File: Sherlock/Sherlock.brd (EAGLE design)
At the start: 91.1 x 58.4 mm, 25 parts, among them U3 XBEE-1B2, X1 2540-

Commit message: Added resistor values for R1-R4 for Sherlock
Change-Id: Ic35e8ce0279ecb8ac04751f8d59191d34fd62b27
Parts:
- R1, R2, R3, R4: value (none) -> 330
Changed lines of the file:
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@@
 <?xml version="1.0" encoding="utf-8"?>
 <!DOCTYPE eagle SYSTEM "eagle.dtd">
-<eagle version="6.2">
+<eagle version="6.3">
 <drawing>
 <settings>
@@
 </class>
 </classes>
-<designrules>
+<designrules name="advancedcircuits-33each-pie">
 <description language="de">&lt;b&gt;EAGLE Design Rules&lt;/b&gt;
 &lt;p&gt;
@@
 <attribute name="VALUE" x="70.485" y="52.07" size="1.27" layer="27" rot="R270"/>
 </element>
-<element name="R1" library="rcl" package="R0603" value="" x="29.21" y="2.54" smashed="yes" rot="MR90">
+<element name="R1" library="rcl" package="R0603" value="330" x="29.21" y="2.54" smashed="yes" rot="MR90">
 <attribute name="NAME" x="30.099" y="7.493" size="1.4224" layer="26" font="vector" ratio="15" rot="MR0"/>
-<attribute name="VALUE" x="27.305" y="1.905" size="1.27" layer="28" rot="MR90"/>
-</element>
-<element name="R2" library="rcl" package="R0603" value="" x="17.78" y="2.54" smashed="yes" rot="MR90">
+<attribute name="VALUE" x="29.845" y="-1.016" size="1.4224" layer="28" rot="MR0"/>
+</element>
+<element name="R2" library="rcl" package="R0603" value="330" x="17.78" y="2.54" smashed="yes" rot="MR90">
 <attribute name="NAME" x="18.669" y="7.62" size="1.4224" layer="26" font="vector" ratio="15" rot="MR0"/>
-<attribute name="VALUE" x="15.875" y="1.905" size="1.27" layer="28" rot="MR90"/>
-</element>
-<element name="R3" library="rcl" package="R0603" value="" x="21.59" y="2.54" smashed="yes" rot="MR90">
+<attribute name="VALUE" x="18.415" y="-1.016" size="1.4224" layer="28" rot="MR0"/>
+</element>
+<element name="R3" library="rcl" package="R0603" value="330" x="21.59" y="2.54" smashed="yes" rot="MR90">
 <attribute name="NAME" x="22.606" y="7.493" size="1.4224" layer="26" font="vector" ratio="15" rot="MR0"/>
-<attribute name="VALUE" x="19.685" y="1.905" size="1.27" layer="28" rot="MR90"/>
-</element>
-<element name="R4" library="rcl" package="R0603" value="" x="25.4" y="2.54" smashed="yes" rot="MR90">
+<attribute name="VALUE" x="22.225" y="-1.016" size="1.4224" layer="28" rot="MR0"/>
+</element>
+<element name="R4" library="rcl" package="R0603" value="330" x="25.4" y="2.54" smashed="yes" rot="MR90">
 <attribute name="NAME" x="26.162" y="7.493" size="1.4224" layer="26" font="vector" ratio="15" rot="MR0"/>
-<attribute name="VALUE" x="23.495" y="1.905" size="1.27" layer="28" rot="MR90"/>
+<attribute name="VALUE" x="26.035" y="-1.016" size="1.4224" layer="28" rot="MR0"/>
 </element>
 <element name="C3" library="rcl" package="C0603K" value=".1uF" x="41.91" y="19.05" smashed="yes" rot="MR0">

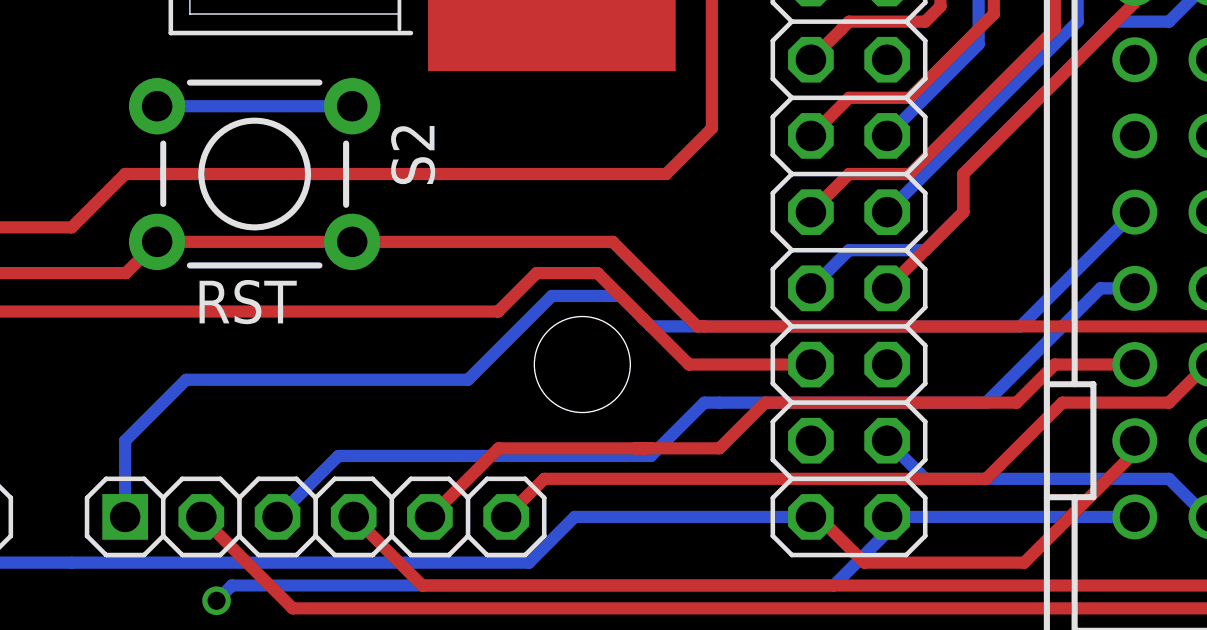
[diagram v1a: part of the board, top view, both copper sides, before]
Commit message: Moved traces away from hole on Sherlock
Change-Id: Icbd6ea3e393f3e41c299999c4f7f65ddeaf7ec65
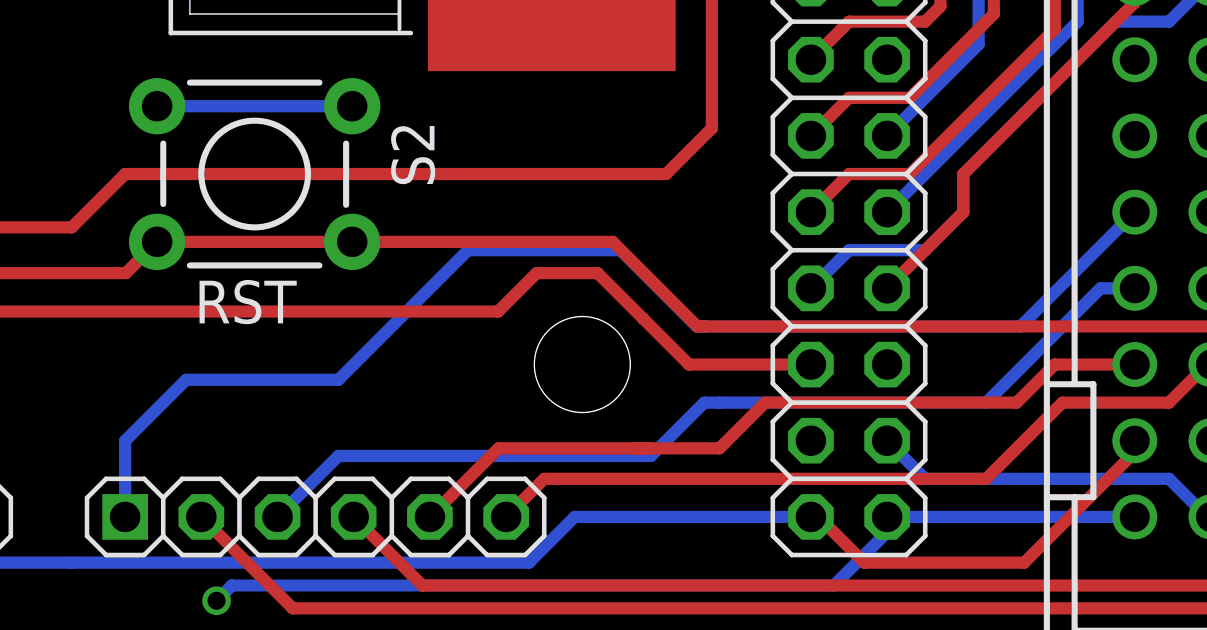
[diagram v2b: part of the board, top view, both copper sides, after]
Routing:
- net ADC0/IO28*: track 40.2 -> 41.5 mm
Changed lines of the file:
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@@
 <grid distance="0.05" unitdist="inch" unit="inch" style="lines" multiple="1" display="yes" altdistance="0.025" altunitdist="inch" altunit="inch"/>
 <layers>
-<layer number="1" name="Top" color="4" fill="1" visible="no" active="yes"/>
+<layer number="1" name="Top" color="4" fill="1" visible="yes" active="yes"/>
 <layer number="16" name="Bottom" color="1" fill="1" visible="yes" active="yes"/>
 <layer number="17" name="Pads" color="2" fill="1" visible="yes" active="yes"/>
@@
 <layer number="19" name="Unrouted" color="6" fill="1" visible="yes" active="yes"/>
 <layer number="20" name="Dimension" color="15" fill="1" visible="yes" active="yes"/>
-<layer number="21" name="tPlace" color="7" fill="1" visible="no" active="yes"/>
+<layer number="21" name="tPlace" color="7" fill="1" visible="yes" active="yes"/>
 <layer number="22" name="bPlace" color="7" fill="1" visible="yes" active="yes"/>
-<layer number="23" name="tOrigins" color="15" fill="1" visible="no" active="yes"/>
+<layer number="23" name="tOrigins" color="15" fill="1" visible="yes" active="yes"/>
 <layer number="24" name="bOrigins" color="15" fill="1" visible="yes" active="yes"/>
-<layer number="25" name="tNames" color="7" fill="1" visible="no" active="yes"/>
+<layer number="25" name="tNames" color="7" fill="1" visible="yes" active="yes"/>
 <layer number="26" name="bNames" color="7" fill="1" visible="yes" active="yes"/>
-<layer number="27" name="tValues" color="7" fill="1" visible="no" active="yes"/>
+<layer number="27" name="tValues" color="7" fill="1" visible="yes" active="yes"/>
 <layer number="28" name="bValues" color="7" fill="1" visible="yes" active="yes"/>
-<layer number="29" name="tStop" color="7" fill="3" visible="no" active="yes"/>
+<layer number="29" name="tStop" color="7" fill="3" visible="yes" active="yes"/>
 <layer number="30" name="bStop" color="7" fill="6" visible="yes" active="yes"/>
-<layer number="31" name="tCream" color="7" fill="4" visible="no" active="yes"/>
+<layer number="31" name="tCream" color="7" fill="4" visible="yes" active="yes"/>
 <layer number="32" name="bCream" color="7" fill="5" visible="yes" active="yes"/>
 <layer number="33" name="tFinish" color="6" fill="3" visible="yes" active="yes"/>
@@
 <param name="mdViaViaSameLayer" value="8mil"/>
 <param name="mnLayersViaInSmd" value="2"/>
-<param name="mdCopperDimension" value="10mil"/>
+<param name="mdCopperDimension" value="25mil"/>
 <param name="mdDrill" value="7mil"/>
 <param name="mdSmdStop" value="0mil"/>
@@
 <contactref element="X1" pad="10"/>
 <wire x1="84.455" y1="12.7" x2="80.645" y2="8.89" width="0.4064" layer="16"/>
-<wire x1="80.645" y1="8.89" x2="68.326" y2="8.89" width="0.4064" layer="16"/>
-<wire x1="68.326" y1="8.89" x2="67.31" y2="9.906" width="0.4064" layer="16"/>
-<wire x1="67.31" y1="9.906" x2="65.024" y2="9.906" width="0.4064" layer="16"/>
-<wire x1="65.024" y1="9.906" x2="62.23" y2="7.112" width="0.4064" layer="16"/>
-<wire x1="62.23" y1="7.112" x2="52.832" y2="7.112" width="0.4064" layer="16"/>
+<wire x1="80.645" y1="8.89" x2="69.85" y2="8.89" width="0.4064" layer="16"/>
+<wire x1="69.85" y1="8.89" x2="68.326" y2="8.89" width="0" layer="19" extent="1-16"/>
 <wire x1="52.832" y1="7.112" x2="50.8" y2="5.08" width="0.4064" layer="16"/>
 <wire x1="50.8" y1="5.08" x2="50.8" y2="2.54" width="0.4064" layer="16"/>
+<wire x1="52.832" y1="7.112" x2="57.912" y2="7.112" width="0.4064" layer="16"/>
+<wire x1="57.912" y1="7.112" x2="62.23" y2="11.43" width="0.4064" layer="16"/>
+<wire x1="62.23" y1="11.43" x2="67.31" y2="11.43" width="0.4064" layer="16"/>
+<wire x1="67.31" y1="11.43" x2="69.85" y2="8.89" width="0.4064" layer="16"/>
 </signal>
 <signal name="PWM5/IO2*">
